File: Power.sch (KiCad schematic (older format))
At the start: 69 parts, among them J3 ESTOP, J4 PWR, J5 Conn_ARM_JTAG_SWD_10, J7 FAN, Q1 MMBT5401LT1G, Q2 PSMN4R8-100BSEJ, Q3 MMBT3904, Q4 Q_NMOS_GDS, Q5 Q_NMOS_GDS, Q6 Q_NMOS_GDS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

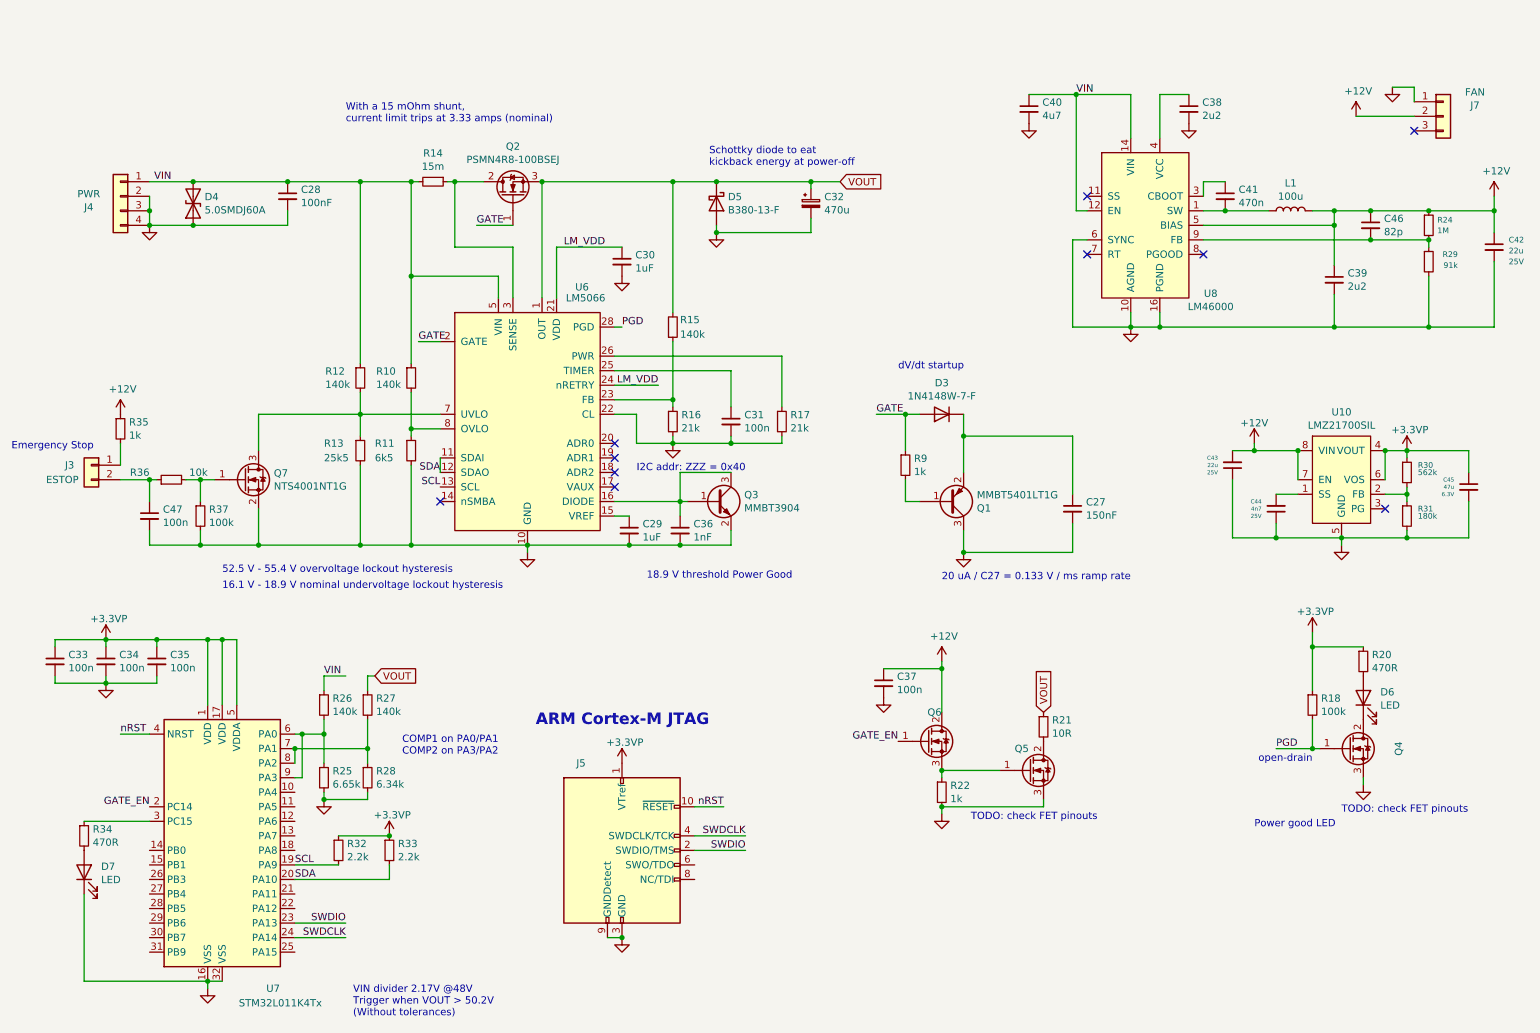
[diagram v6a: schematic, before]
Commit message: WIP 48v-12v dc/dc converter tweaks. need to restore to BLDC values
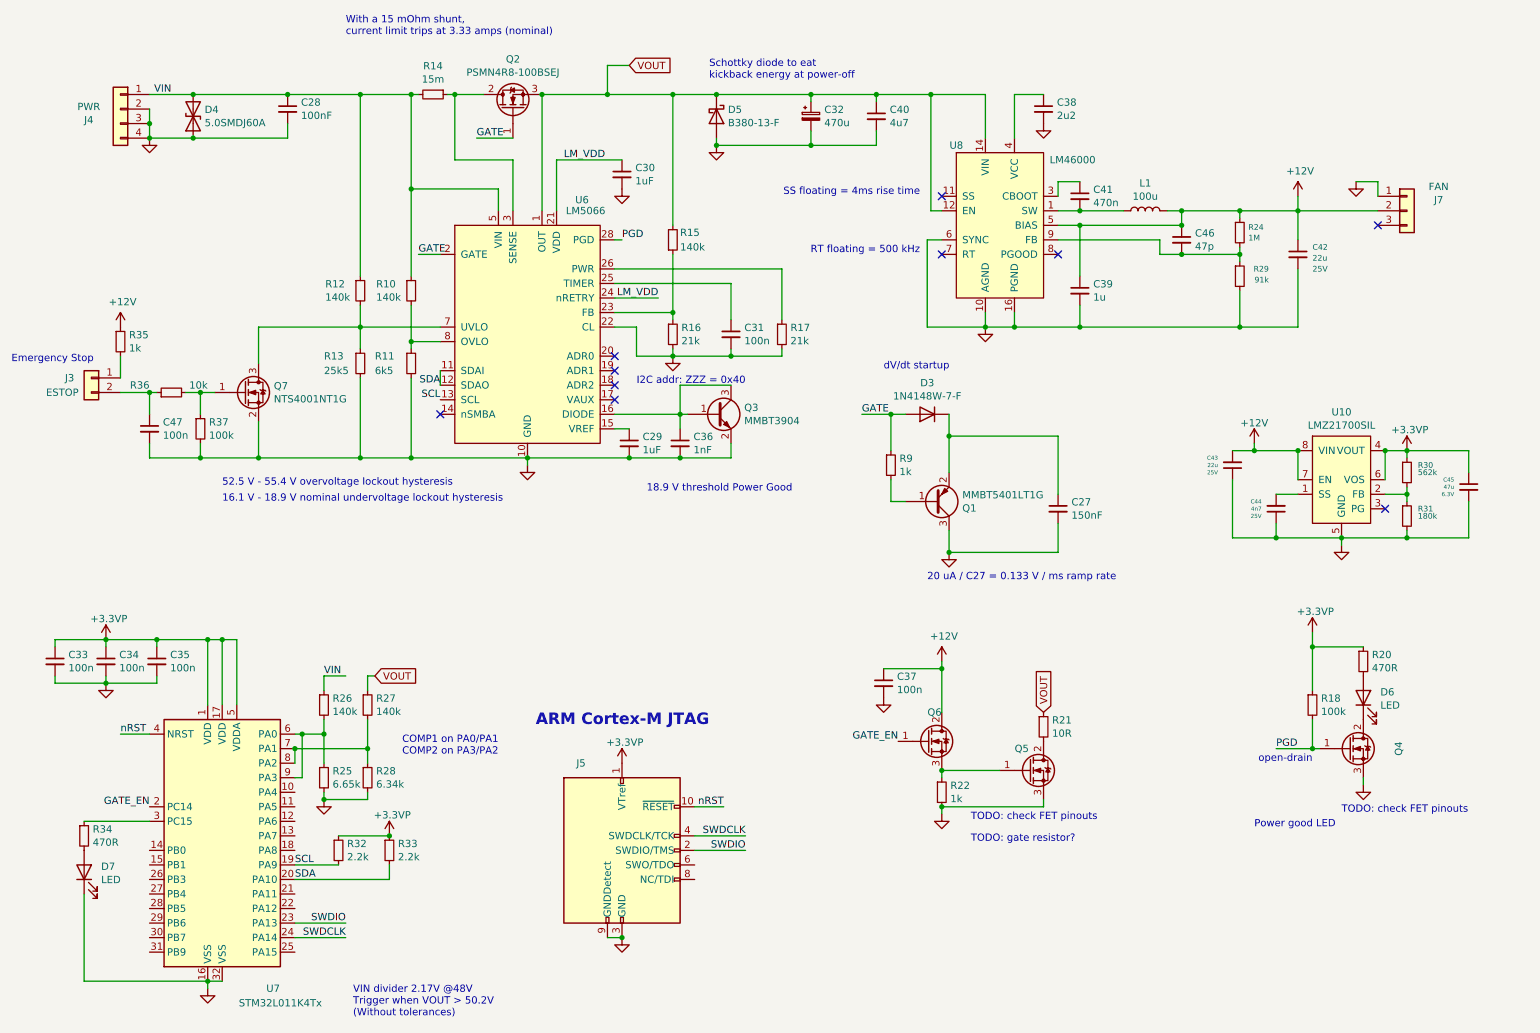
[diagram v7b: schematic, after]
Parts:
- C39: value 2u2 -> 1u
- C46: value 82p -> 47p
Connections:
- net VIN: no longer C40.1, U8.12 (EN), U8.13 (VIN), U8.14 (VIN)
- net VOUT: now also C40.1, U8.12 (EN), U8.13 (VIN), U8.14 (VIN)
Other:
- note added: "RT floating = 500 kHz"
- note added: "SS floating = 4ms rise time"
- note added: "TODO: gate resistor?"
- moved on the sheet: C27, C28, C29, C30, C31, C32, C36, C38, C39, C40, C41, C42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

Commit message: add MCU reset cap, tweak dc-dc feedback divider
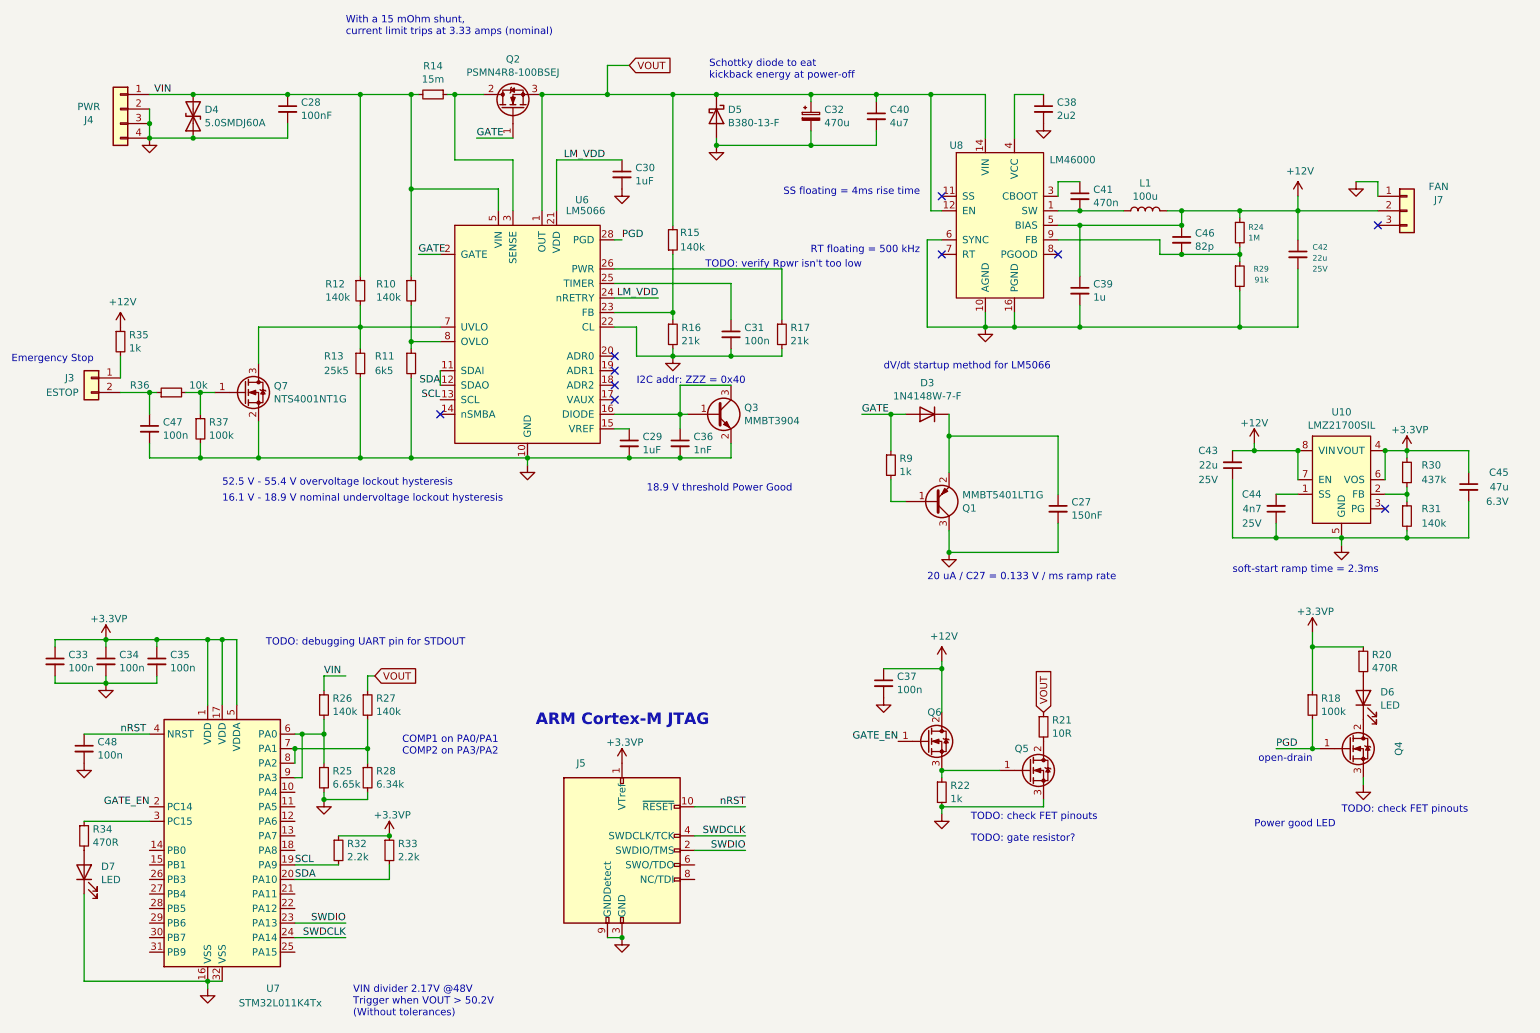
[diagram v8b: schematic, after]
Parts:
- added C48: 100n, Capacitor_SMD:C_0603_1608Metric, symbol Device:C_Small
- C46: value 47p -> 82p
- R30: value 562k -> 437k; D1PN YAG3212CT-ND -> P432KHCT-ND; MFN Yageo -> Panasonic; MPN RC0402FR-07681KL -> ERJ-3EKF4323V; Maximum Power 0.0625W -> (none); Resistance 681000.0ohm -> 432000
- R31: value 180k -> 140k; D1PN 311-180KLRCT-ND -> (none); MFN Yageo -> (none); MPN RC0402FR-07180KL -> (none); Maximum Power 0.0625W -> (none); Resistance 180000.0ohm -> (none)
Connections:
- net GND: now also C48.2
- net nRST: now also C48.1
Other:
- note added: "TODO: debugging UART pin for STDOUT"
- note added: "TODO: verify Rpwr isn't too low"
- note added: "dV/dt startup method for LM5066"
- note added: "soft-start ramp time = 2.3ms"
- note removed: "dV/dt startup"
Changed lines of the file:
@@
 	900  5150 1250 5150
 Wire Wire Line
+	1100 5500 1550 5500
+Wire Wire Line
 	1100 6600 1100 7200
 Wire Wire Line
@@
 	1350 3150 1550 3150
 Wire Wire Line
-	1350 5500 1550 5500
-Wire Wire Line
 	1550 1100 1850 1100
 Wire Wire Line
@@
 	5250 3300 5200 3300
 Wire Wire Line
-	5300 6000 5500 6000
+	5300 6000 5650 6000
 Wire Wire Line
 	5450 1100 6100 1100
@@
 Text Notes 2050 3910 0    50   ~ 0
 16.1 V - 18.9 V nominal undervoltage lockout hysteresis
+Text Notes 2350 4900 0    50   ~ 0
+TODO: debugging UART pin for STDOUT
 Text Notes 2900 700  0    50   ~ 0
 With a 15 mOhm shunt,\ncurrent limit trips at 3.33 amps (nominal)
@@
 Text Notes 5650 3100 2    50   ~ 0
 I2C addr: ZZZ = 0x40
+Text Notes 6450 2300 2    50   ~ 0
+TODO: verify Rpwr isn't too low
 Text Notes 6600 3000 0    50   ~ 0
-dV/dt startup
+dV/dt startup method for LM5066
 Text Notes 6850 1800 2    50   ~ 0
 SS floating = 4ms rise time
@@
 Text Notes 8200 4450 2    50   ~ 0
 20 uA / C27 = 0.133 V / ms ramp rate
+Text Notes 9000 4400 0    50   ~ 0
+soft-start ramp time = 2.3ms
 Text Notes 9150 6150 0    50   ~ 0
 Power good LED
@@
 Text Label 5050 2500 2    50   ~ 0
 LM_VDD
-Text Label 5500 6000 2    50   ~ 0
+Text Label 5650 6000 2    50   ~ 0
 nRST
 Text Label 5650 6200 2    50   ~ 0
@@
 $EndComp
 $Comp
+L power:GND #PWR0138
+U 1 1 5E53895F
+P 1100 5700
+F 0 "#PWR0138" H 1100 5450 50  0001 C CNN
+F 1 "GND" H 1105 5527 50  0001 C CNN
+F 2 "" H 1100 5700 50  0001 C CNN
+F 3 "" H 1100 5700 50  0001 C CNN
+	1    1100 5700
+	-1   0    0    -1
+$EndComp
+$Comp
 L power:GND #PWR0137
 U 1 1 5E51A5F9
@@
 U 1 1 5D6A675C
 P 10200 3700
-F 0 "R30" H 10275 3750 39  0000 L CNN
-F 1 "562k" H 10275 3700 39  0000 L CNN
+F 0 "R30" H 10300 3750 50  0000 L CNN
+F 1 "437k" H 10300 3650 50  0000 L CNN
 F 2 "Resistor_SMD:R_0402_1005Metric" H 10200 3700 60  0001 C CNN
 F 3 "~" H 10200 3700 60  0001 C CNN
 F 4 "Digikey" H 10250 3800 50  0001 C CNN "D1N"
-F 5 "YAG3212CT-ND " H 10250 3800 50  0001 C CNN "D1PN"
-F 6 "Yageo" H 10250 3800 50  0001 C CNN "MFN"
-F 7 "RC0402FR-07681KL" H 10250 3800 50  0001 C CNN "MPN"
-F 8 "0.0625W" H 10200 3700 60  0001 C CNN "Maximum Power"
-F 9 "681000.0ohm" H 10200 3700 60  0001 C CNN "Resistance"
+F 5 "P432KHCT-ND" H 10250 3800 50  0001 C CNN "D1PN"
+F 6 "Panasonic" H 10250 3800 50  0001 C CNN "MFN"
+F 7 "ERJ-3EKF4323V" H 10250 3800 50  0001 C CNN "MPN"
+F 8 "" H 10200 3700 60  0001 C CNN "Maximum Power"
+F 9 "432000" H 10200 3700 60  0001 C CNN "Resistance"
 F 10 "1%" H 10200 3700 60  0001 C CNN "Tolerance"
 	1    10200 3700
@@
 U 1 1 5D6A675D
 P 10200 4000
-F 0 "R31" H 10275 4050 39  0000 L CNN
-F 1 "180k" H 10275 4000 39  0000 L CNN
+F 0 "R31" H 10300 4050 50  0000 L CNN
+F 1 "140k" H 10300 3950 50  0000 L CNN
 F 2 "Resistor_SMD:R_0402_1005Metric" H 10200 4000 60  0001 C CNN
 F 3 "~" H 10200 4000 60  0001 C CNN
 F 4 "Digikey" H 10250 4100 50  0001 C CNN "D1N"
-F 5 "311-180KLRCT-ND " H 10250 4100 50  0001 C CNN "D1PN"
-F 6 "Yageo" H 10250 4100 50  0001 C CNN "MFN"
-F 7 "RC0402FR-07180KL" H 10250 4100 50  0001 C CNN "MPN"
-F 8 "0.0625W" H 10200 4000 60  0001 C CNN "Maximum Power"
-F 9 "180000.0ohm" H 10200 4000 60  0001 C CNN "Resistance"
+F 5 "" H 10250 4100 50  0001 C CNN "D1PN"
+F 6 "" H 10250 4100 50  0001 C CNN "MFN"
+F 7 "" H 10250 4100 50  0001 C CNN "MPN"
+F 8 "" H 10200 4000 60  0001 C CNN "Maximum Power"
+F 9 "" H 10200 4000 60  0001 C CNN "Resistance"
 F 10 "1%" H 10200 4000 60  0001 C CNN "Tolerance"
 	1    10200 4000
@@
 $EndComp
 $Comp
+L Device:C_Small C48
+U 1 1 5E5381D4
+P 1100 5600
+F 0 "C48" H 1192 5646 50  0000 L CNN
+F 1 "100n" H 1192 5555 50  0000 L CNN
+F 2 "Capacitor_SMD:C_0603_1608Metric" H 1100 5600 50  0001 C CNN
+F 3 "~" H 1100 5600 50  0001 C CNN
+	1    1100 5600
+	1    0    0    -1
+$EndComp
+$Comp
 L Device:C_Small C34
 U 1 1 5D513ABF
@@
 P 8650 2100
 F 0 "C46" H 8742 2146 50  0000 L CNN
-F 1 "47p" H 8742 2055 50  0000 L CNN
+F 1 "82p" H 8742 2055 50  0000 L CNN
 F 2 "Capacitor_SMD:C_0603_1608Metric" H 8650 2100 50  0001 C CNN
 F 3 "~" H 8650 2100 50  0001 C CNN
@@
 U 1 1 5D6A675A
 P 9000 3650
-F 0 "C43" H 9100 3600 28  0000 L CNN
-F 1 "22u" H 9100 3650 28  0000 L CNN
+F 0 "C43" H 9100 3550 50  0000 L CNN
+F 1 "22u" H 9100 3650 50  0000 L CNN
 F 2 "Capacitor_SMD:C_1206_3216Metric" H 9000 3650 60  0001 C CNN
 F 3 "~" H 9000 3650 60  0001 C CNN
@@
 F 7 "Samsung" H 9100 3700 50  0001 C CNN "MFN"
 F 8 "CL32A226KAJNNNE" H 9100 3700 50  0001 C CNN "MPN"
-F 9 "25V" H 9100 3700 28  0000 L CNN "Maximum Voltage"
+F 9 "25V" H 9100 3750 50  0000 L CNN "Maximum Voltage"
 F 10 "10%" H 9000 3650 60  0001 C CNN "Tolerance"
 	1    9000 3650
@@
 U 1 1 5D6A675B
 P 9300 3950
-F 0 "C44" H 9400 3900 28  0000 L CNN
-F 1 "4n7" H 9400 3950 28  0000 L CNN
+F 0 "C44" H 9400 3850 50  0000 L CNN
+F 1 "4n7" H 9400 3950 50  0000 L CNN
 F 2 "Capacitor_SMD:C_0402_1005Metric" H 9300 3950 60  0001 C CNN
 F 3 "~" H 9300 3950 60  0001 C CNN
@@
 F 7 "Yageo" H 9400 4000 50  0001 C CNN "MFN"
 F 8 "CC0402KRX7R8BB472" H 9400 4000 50  0001 C CNN "MPN"
-F 9 "25V" H 9400 4000 28  0000 L CNN "Maximum Voltage"
+F 9 "25V" H 9400 4050 50  0000 L CNN "Maximum Voltage"
 F 10 "10%" H 9300 3950 60  0001 C CNN "Tolerance"
 	1    9300 3950
@@
 U 1 1 5D6A6760
 P 10625 3800
-F 0 "C45" H 10725 3850 28  0000 L CNN
-F 1 "47u" H 10725 3800 28  0000 L CNN
+F 0 "C45" H 10350 3900 50  0000 L CNN
+F 1 "47u" H 10350 3800 50  0000 L CNN
 F 2 "Capacitor_SMD:C_1206_3216Metric" H 10625 3800 60  0001 C CNN
 F 3 "~" H 10625 3800 60  0001 C CNN
@@
 F 7 "Samsung" H 10725 3850 50  0001 C CNN "MFN"
 F 8 "CL32A226KAJNNNE" H 10725 3850 50  0001 C CNN "MPN"
-F 9 "6.3V" H 10725 3750 28  0000 L CNN "Maximum Voltage"
+F 9 "6.3V" H 10350 3700 50  0000 L CNN "Maximum Voltage"
 F 10 "10%" H 10625 3800 60  0001 C CNN "Tolerance"
 	1    10625 3800
